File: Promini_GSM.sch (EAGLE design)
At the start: 8 parts, among them IC1 EL357N-B-TA-G

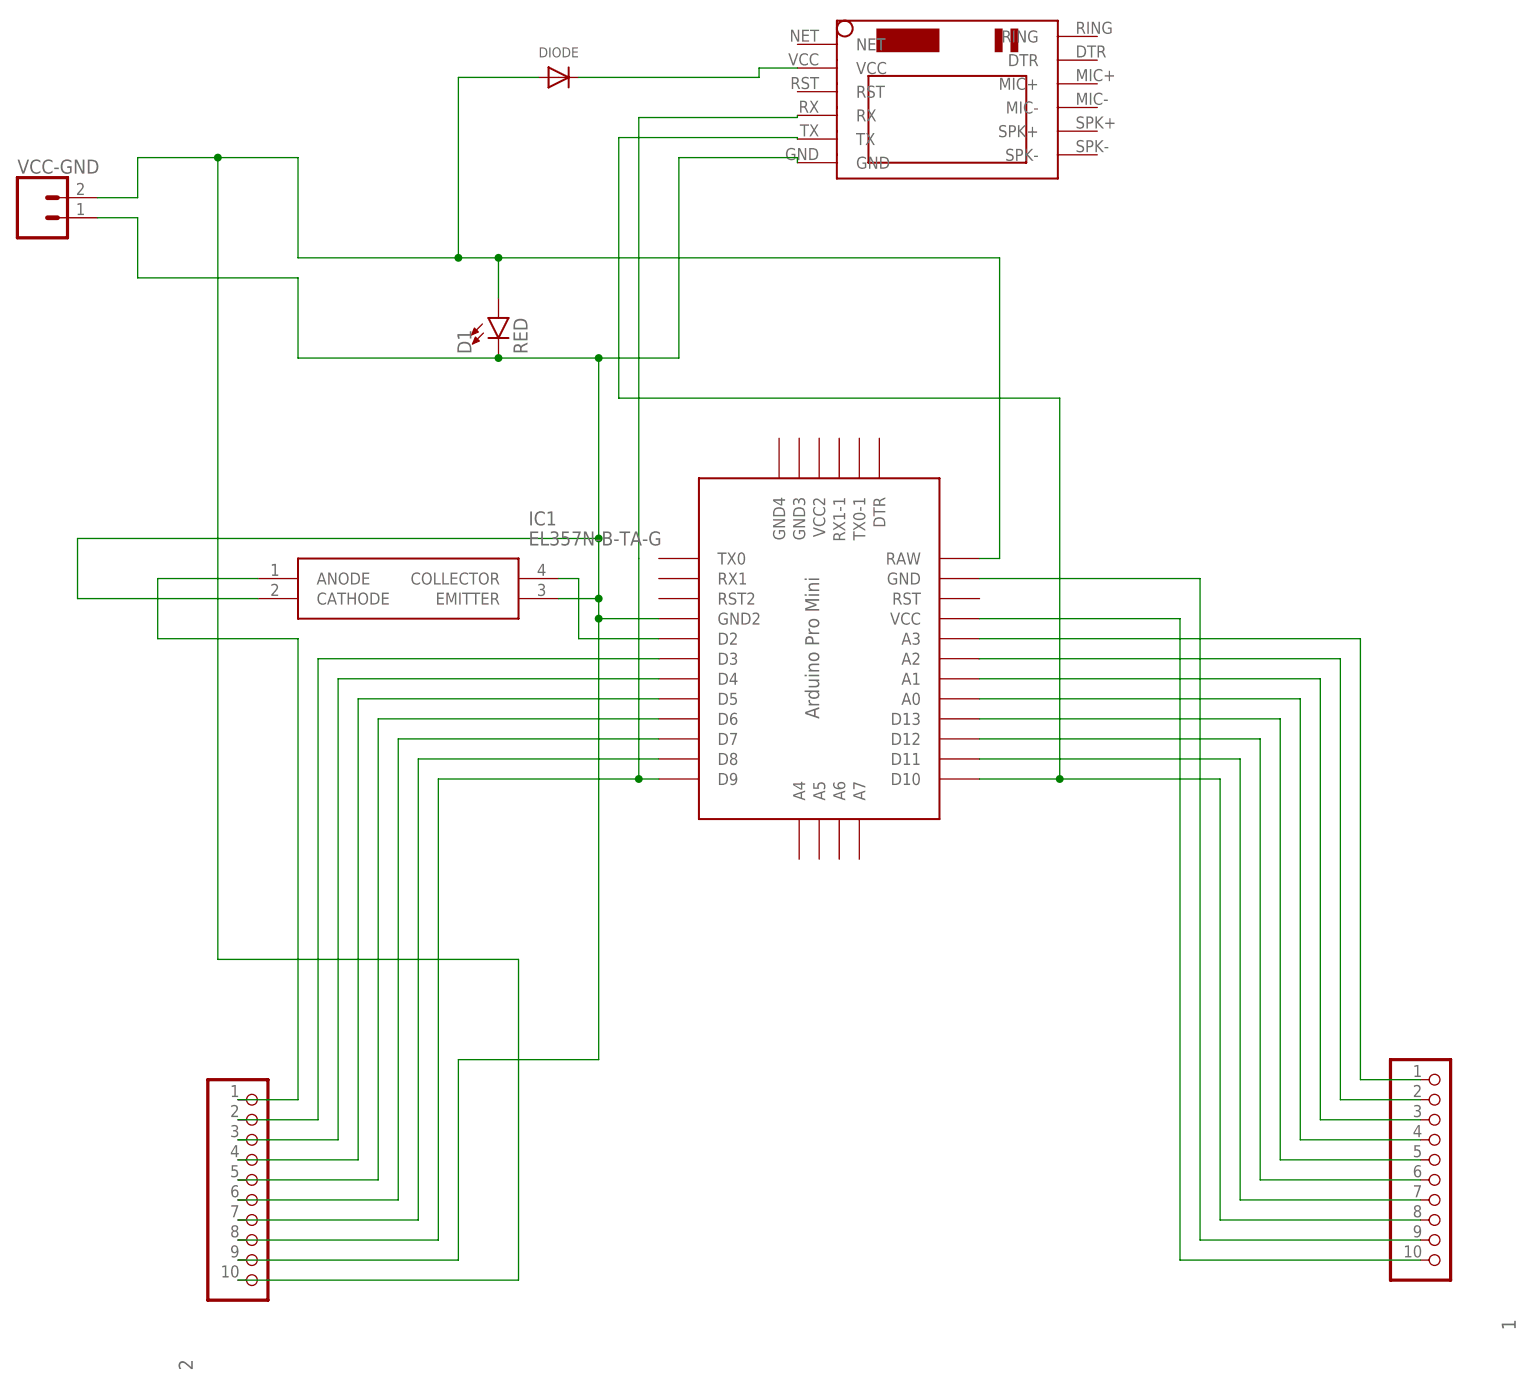
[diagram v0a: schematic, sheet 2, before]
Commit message: tx rx and rst line added
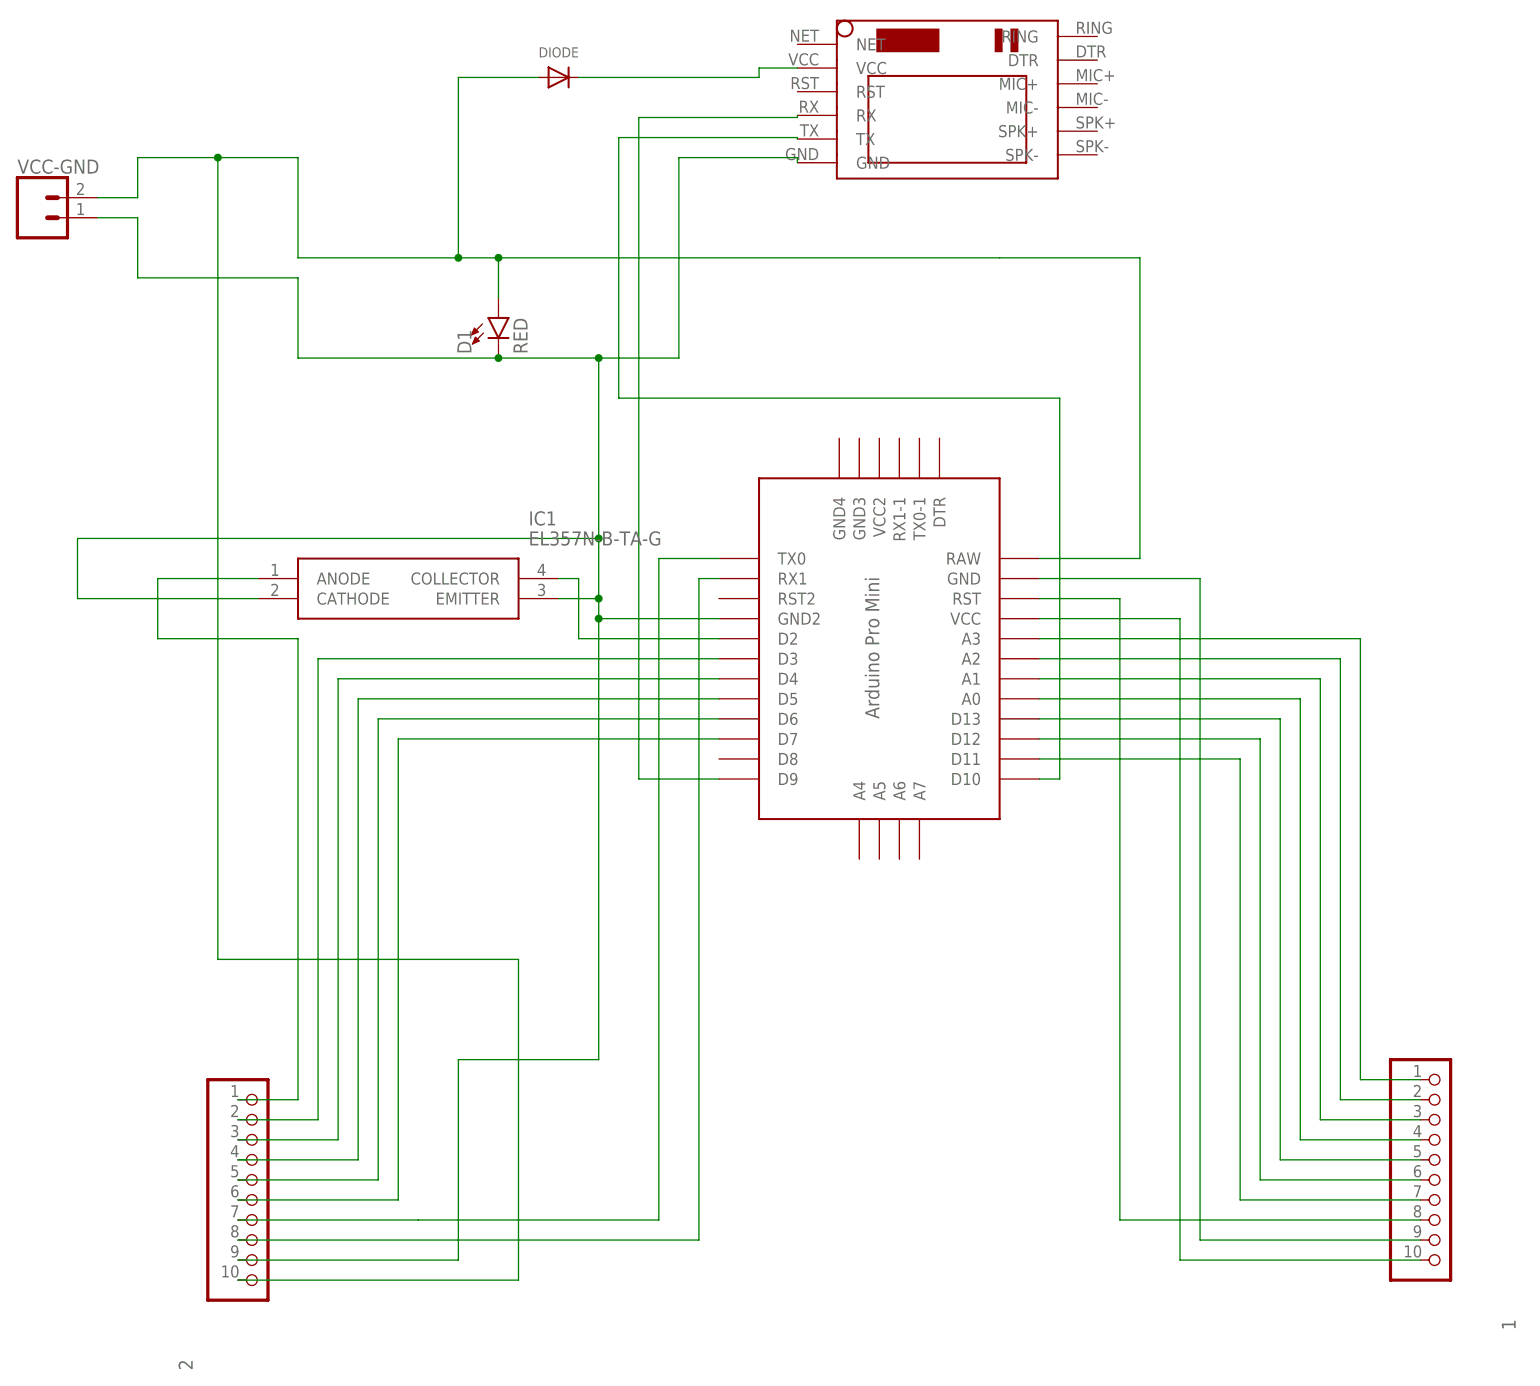
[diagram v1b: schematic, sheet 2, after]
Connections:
- new net N$13: 1.8, PROMINI.RST
- new net N$2: 2.8, PROMINI.RX1
- net N$14: now also PROMINI.TX0; no longer PROMINI.D8
- net N$23: no longer 1.8
- net N$6: no longer 2.8
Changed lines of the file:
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@@
 </plain>
 <instances>
-<instance part="PROMINI" gate="G$1" x="81.28" y="73.66" smashed="yes"/>
+<instance part="PROMINI" gate="G$1" x="88.9" y="73.66" smashed="yes"/>
 <instance part="2" gate="A" x="7.62" y="15.24" smashed="yes">
 <attribute name="NAME" x="-0.635" y="-8.89" size="1.778" layer="95" rot="R90"/>
@@
 <wire x1="38.1" y1="132.08" x2="38.1" y2="127" width="0.762" layer="91"/>
 <junction x="38.1" y="132.08"/>
-<pinref part="PROMINI" gate="G$1" pin="RAW"/>
 <wire x1="38.1" y1="132.08" x2="101.6" y2="132.08" width="0.762" layer="91"/>
-<wire x1="101.6" y1="132.08" x2="101.6" y2="93.98" width="0.762" layer="91"/>
-<wire x1="101.6" y1="93.98" x2="99.06" y2="93.98" width="0.762" layer="91"/>
 <pinref part="DIODE" gate="G$1" pin="A"/>
 <pinref part="D1" gate="G$1" pin="A"/>
@@
 <wire x1="-12.7" y1="139.7" x2="-7.62" y2="139.7" width="0.762" layer="91"/>
 <wire x1="-7.62" y1="139.7" x2="-7.62" y2="144.78" width="0.762" layer="91"/>
+<wire x1="101.6" y1="132.08" x2="119.38" y2="132.08" width="0.1524" layer="91"/>
+<wire x1="119.38" y1="132.08" x2="119.38" y2="93.98" width="0.1524" layer="91"/>
+<pinref part="PROMINI" gate="G$1" pin="RAW"/>
+<wire x1="119.38" y1="93.98" x2="106.68" y2="93.98" width="0.1524" layer="91"/>
 </segment>
 </net>
@@
 <segment>
 <wire x1="75.98" y1="149.86" x2="55.88" y2="149.86" width="0.762" layer="91"/>
-<wire x1="55.88" y1="149.86" x2="55.88" y2="93.98" width="0.762" layer="91"/>
+<wire x1="55.88" y1="149.86" x2="55.88" y2="66.04" width="0.762" layer="91"/>
 <pinref part="U$1" gate="G$1" pin="RX"/>
 <wire x1="75.98" y1="150.13" x2="75.98" y2="149.86" width="0.762" layer="91"/>
 <pinref part="PROMINI" gate="G$1" pin="D9"/>
-<wire x1="58.42" y1="66.04" x2="55.88" y2="66.04" width="0.762" layer="91"/>
-<wire x1="55.88" y1="66.04" x2="30.48" y2="66.04" width="0.762" layer="91"/>
-<wire x1="30.48" y1="66.04" x2="30.48" y2="7.62" width="0.762" layer="91"/>
-<pinref part="2" gate="A" pin="8"/>
-<wire x1="30.48" y1="7.62" x2="5.08" y2="7.62" width="0.762" layer="91"/>
-<wire x1="55.88" y1="93.98" x2="55.88" y2="66.04" width="0.762" layer="91"/>
-<junction x="55.88" y="66.04"/>
+<wire x1="66.04" y1="66.04" x2="55.88" y2="66.04" width="0.762" layer="91"/>
 </segment>
 </net>
@@
 <segment>
 <pinref part="PROMINI" gate="G$1" pin="D3"/>
-<wire x1="58.42" y1="81.28" x2="15.24" y2="81.28" width="0.762" layer="91"/>
+<wire x1="66.04" y1="81.28" x2="15.24" y2="81.28" width="0.762" layer="91"/>
 <wire x1="15.24" y1="81.28" x2="15.24" y2="22.86" width="0.762" layer="91"/>
 <pinref part="2" gate="A" pin="2"/>
@@
 <segment>
 <pinref part="PROMINI" gate="G$1" pin="D4"/>
-<wire x1="58.42" y1="78.74" x2="17.78" y2="78.74" width="0.762" layer="91"/>
+<wire x1="66.04" y1="78.74" x2="17.78" y2="78.74" width="0.762" layer="91"/>
 <wire x1="17.78" y1="78.74" x2="17.78" y2="20.32" width="0.762" layer="91"/>
 <pinref part="2" gate="A" pin="3"/>
@@
 <segment>
 <pinref part="PROMINI" gate="G$1" pin="D5"/>
-<wire x1="58.42" y1="76.2" x2="20.32" y2="76.2" width="0.762" layer="91"/>
+<wire x1="66.04" y1="76.2" x2="20.32" y2="76.2" width="0.762" layer="91"/>
 <pinref part="2" gate="A" pin="4"/>
 <wire x1="20.32" y1="76.2" x2="20.32" y2="17.78" width="0.762" layer="91"/>
@@
 <segment>
 <pinref part="PROMINI" gate="G$1" pin="D6"/>
-<wire x1="58.42" y1="73.66" x2="22.86" y2="73.66" width="0.762" layer="91"/>
+<wire x1="66.04" y1="73.66" x2="22.86" y2="73.66" width="0.762" layer="91"/>
 <wire x1="22.86" y1="73.66" x2="22.86" y2="15.24" width="0.762" layer="91"/>
 <pinref part="2" gate="A" pin="5"/>
@@
 <segment>
 <pinref part="PROMINI" gate="G$1" pin="D7"/>
-<wire x1="58.42" y1="71.12" x2="25.4" y2="71.12" width="0.762" layer="91"/>
+<wire x1="66.04" y1="71.12" x2="25.4" y2="71.12" width="0.762" layer="91"/>
 <wire x1="25.4" y1="71.12" x2="25.4" y2="12.7" width="0.762" layer="91"/>
 <pinref part="2" gate="A" pin="6"/>
@@
 <net name="N$14" class="0">
 <segment>
-<pinref part="PROMINI" gate="G$1" pin="D8"/>
-<wire x1="58.42" y1="68.58" x2="27.94" y2="68.58" width="0.762" layer="91"/>
-<wire x1="27.94" y1="68.58" x2="27.94" y2="10.16" width="0.762" layer="91"/>
 <pinref part="2" gate="A" pin="7"/>
 <wire x1="27.94" y1="10.16" x2="5.08" y2="10.16" width="0.762" layer="91"/>
+<pinref part="PROMINI" gate="G$1" pin="TX0"/>
+<wire x1="66.04" y1="93.98" x2="58.42" y2="93.98" width="0.1524" layer="91"/>
+<wire x1="58.42" y1="93.98" x2="58.42" y2="10.16" width="0.1524" layer="91"/>
+<wire x1="58.42" y1="10.16" x2="27.94" y2="10.16" width="0.1524" layer="91"/>
 </segment>
 </net>
@@
 <segment>
 <pinref part="PROMINI" gate="G$1" pin="A3"/>
-<wire x1="99.06" y1="83.82" x2="147.32" y2="83.82" width="0.762" layer="91"/>
+<wire x1="106.68" y1="83.82" x2="147.32" y2="83.82" width="0.762" layer="91"/>
 <wire x1="147.32" y1="83.82" x2="147.32" y2="27.94" width="0.762" layer="91"/>
 <pinref part="1" gate="A" pin="1"/>
@@
 <segment>
 <pinref part="PROMINI" gate="G$1" pin="A2"/>
-<wire x1="99.06" y1="81.28" x2="144.78" y2="81.28" width="0.762" layer="91"/>
+<wire x1="106.68" y1="81.28" x2="144.78" y2="81.28" width="0.762" layer="91"/>
 <wire x1="144.78" y1="81.28" x2="144.78" y2="25.4" width="0.762" layer="91"/>
 <pinref part="1" gate="A" pin="2"/>
@@
 <segment>
 <pinref part="PROMINI" gate="G$1" pin="A1"/>
-<wire x1="99.06" y1="78.74" x2="142.24" y2="78.74" width="0.762" layer="91"/>
+<wire x1="106.68" y1="78.74" x2="142.24" y2="78.74" width="0.762" layer="91"/>
 <pinref part="1" gate="A" pin="3"/>
 <wire x1="142.24" y1="78.74" x2="142.24" y2="22.86" width="0.762" layer="91"/>
@@
 <segment>
 <pinref part="PROMINI" gate="G$1" pin="A0"/>
-<wire x1="99.06" y1="76.2" x2="139.7" y2="76.2" width="0.762" layer="91"/>
+<wire x1="106.68" y1="76.2" x2="139.7" y2="76.2" width="0.762" layer="91"/>
 <wire x1="139.7" y1="76.2" x2="139.7" y2="20.32" width="0.762" layer="91"/>
 <pinref part="1" gate="A" pin="4"/>
@@
 <segment>
 <pinref part="PROMINI" gate="G$1" pin="D13"/>
-<wire x1="99.06" y1="73.66" x2="137.16" y2="73.66" width="0.762" layer="91"/>
+<wire x1="106.68" y1="73.66" x2="137.16" y2="73.66" width="0.762" layer="91"/>
 <pinref part="1" gate="A" pin="5"/>
 <wire x1="137.16" y1="73.66" x2="137.16" y2="17.78" width="0.762" layer="91"/>
@@
 <segment>
 <pinref part="PROMINI" gate="G$1" pin="D12"/>
-<wire x1="99.06" y1="71.12" x2="134.62" y2="71.12" width="0.762" layer="91"/>
+<wire x1="106.68" y1="71.12" x2="134.62" y2="71.12" width="0.762" layer="91"/>
 <pinref part="1" gate="A" pin="6"/>
 <wire x1="134.62" y1="71.12" x2="134.62" y2="15.24" width="0.762" layer="91"/>
@@
 <segment>
 <pinref part="PROMINI" gate="G$1" pin="D11"/>
-<wire x1="99.06" y1="68.58" x2="132.08" y2="68.58" width="0.762" layer="91"/>
+<wire x1="106.68" y1="68.58" x2="132.08" y2="68.58" width="0.762" layer="91"/>
 <wire x1="132.08" y1="68.58" x2="132.08" y2="12.7" width="0.762" layer="91"/>
 <pinref part="1" gate="A" pin="7"/>
@@
 <segment>
 <pinref part="PROMINI" gate="G$1" pin="D10"/>
-<wire x1="99.06" y1="66.04" x2="109.22" y2="66.04" width="0.762" layer="91"/>
-<wire x1="109.22" y1="66.04" x2="129.54" y2="66.04" width="0.762" layer="91"/>
-<wire x1="129.54" y1="66.04" x2="129.54" y2="10.16" width="0.762" layer="91"/>
-<pinref part="1" gate="A" pin="8"/>
-<wire x1="129.54" y1="10.16" x2="154.94" y2="10.16" width="0.762" layer="91"/>
+<wire x1="106.68" y1="66.04" x2="109.22" y2="66.04" width="0.762" layer="91"/>
 <wire x1="109.22" y1="66.04" x2="109.22" y2="114.3" width="0.762" layer="91"/>
-<junction x="109.22" y="66.04"/>
 <wire x1="75.98" y1="147.32" x2="53.34" y2="147.32" width="0.762" layer="91"/>
 <wire x1="53.34" y1="147.32" x2="53.34" y2="114.3" width="0.762" layer="91"/>
@@
 <segment>
 <pinref part="PROMINI" gate="G$1" pin="GND"/>
-<wire x1="99.06" y1="91.44" x2="127" y2="91.44" width="0.762" layer="91"/>
+<wire x1="106.68" y1="91.44" x2="127" y2="91.44" width="0.762" layer="91"/>
 <wire x1="127" y1="91.44" x2="127" y2="7.62" width="0.762" layer="91"/>
 <pinref part="1" gate="A" pin="9"/>
@@
 <segment>
 <pinref part="PROMINI" gate="G$1" pin="GND2"/>
-<wire x1="50.8" y1="86.36" x2="58.42" y2="86.36" width="0.762" layer="91"/>
+<wire x1="50.8" y1="86.36" x2="66.04" y2="86.36" width="0.762" layer="91"/>
 <wire x1="50.8" y1="86.36" x2="50.8" y2="30.48" width="0.762" layer="91"/>
 <wire x1="50.8" y1="30.48" x2="33.02" y2="30.48" width="0.762" layer="91"/>
@@
 <pinref part="1" gate="A" pin="10"/>
 <pinref part="PROMINI" gate="G$1" pin="VCC"/>
-<wire x1="99.06" y1="86.36" x2="124.46" y2="86.36" width="0.762" layer="91"/>
+<wire x1="106.68" y1="86.36" x2="124.46" y2="86.36" width="0.762" layer="91"/>
 <wire x1="124.46" y1="86.36" x2="124.46" y2="5.08" width="0.762" layer="91"/>
 <wire x1="124.46" y1="5.08" x2="154.94" y2="5.08" width="0.762" layer="91"/>
@@
 <segment>
 <pinref part="PROMINI" gate="G$1" pin="D2"/>
-<wire x1="58.42" y1="83.82" x2="48.26" y2="83.82" width="0.762" layer="91"/>
+<wire x1="66.04" y1="83.82" x2="48.26" y2="83.82" width="0.762" layer="91"/>
 <pinref part="IC1" gate="G$1" pin="COLLECTOR"/>
 <wire x1="45.72" y1="91.44" x2="48.26" y2="91.44" width="0.762" layer="91"/>
@@
 </segment>
 </net>
+<net name="N$2" class="0">
+<segment>
+<pinref part="PROMINI" gate="G$1" pin="RX1"/>
+<wire x1="66.04" y1="91.44" x2="63.5" y2="91.44" width="0.1524" layer="91"/>
+<wire x1="63.5" y1="91.44" x2="63.5" y2="7.62" width="0.1524" layer="91"/>
+<pinref part="2" gate="A" pin="8"/>
+<wire x1="63.5" y1="7.62" x2="5.08" y2="7.62" width="0.1524" layer="91"/>
+</segment>
+</net>
+<net name="N$13" class="0">
+<segment>
+<pinref part="PROMINI" gate="G$1" pin="RST"/>
+<wire x1="106.68" y1="88.9" x2="116.84" y2="88.9" width="0.1524" layer="91"/>
+<pinref part="1" gate="A" pin="8"/>
+<wire x1="116.84" y1="88.9" x2="116.84" y2="10.16" width="0.1524" layer="91"/>
+<wire x1="116.84" y1="10.16" x2="154.94" y2="10.16" width="0.1524" layer="91"/>
+</segment>
+</net>
